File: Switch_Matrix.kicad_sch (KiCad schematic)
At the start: 151 parts, among them SW1 SW_Push_45deg, SW10 SW_Push_45deg, SW11 SW_Push_45deg, SW12 SW_Push_45deg, SW12(2)1 SW_Push_45deg, SW13 SW_Push_45deg, SW14 SW_Push_45deg, SW15 SW_Push_45deg, SW16 SW_Push_45deg, SW17 SW_Push_45deg, SW18 SW_Push_45deg, SW19 SW_Push_45deg, SW2 SW_Push_45deg, SW20 SW_Push_45deg, SW21 SW_Push_45deg, SW22 SW_Push_45deg, SW23 SW_Push_45deg, SW24 SW_Push_45deg, SW24(1.5)1 SW_Push_45deg, SW25 SW_Push_45deg, SW26 SW_Push_45deg, SW26(2)1 SW_Push_45deg, SW26(ISO)1 SW_Push_45deg, SW27(1.25)1 SW_Push_45deg, SW27(1.5)1 SW_Push_45deg, SW27(ortho)1 SW_Push_45deg, SW28 SW_Push_45deg, SW28(1.5stagger)1 SW_Push_45deg, SW28(ortho)1 SW_Push_45deg, SW29 SW_Push_45deg, SW29(1.5stagger)1 SW_Push_45deg, SW29(ortho)1 SW_Push_45deg, SW3 SW_Push_45deg, SW30 SW_Push_45deg, SW30(1.5stagger)1 SW_Push_45deg, SW30(ortho)1 SW_Push_45deg, SW31 SW_Push_45deg, SW31(1.5stagger)1 SW_Push_45deg, SW31(ortho)1 SW_Push_45deg, SW32 SW_Push_45deg, SW32(1.5stagger)1 SW_Push_45deg, SW32(ortho)1 SW_Push_45deg, SW33 SW_Push_45deg, SW33(1.5stagger)1 SW_Push_45deg, SW33(ortho)1 SW_Push_45deg, SW34 SW_Push_45deg, SW34(1.5stagger)1 SW_Push_45deg, SW34(ortho)1 SW_Push_45deg, SW35 SW_Push_45deg, SW35(1.5stagger)1 SW_Push_45deg, SW35(ortho)1 SW_Push_45deg, SW36 SW_Push_45deg, SW36(1.5stagger)1 SW_Push_45deg, SW36(ortho)1 SW_Push_45deg, SW37 SW_Push_45deg, SW37(1.5stagger)1 SW_Push_45deg, SW37(ortho)1 SW_Push_45deg, SW38(1.25)1 SW_Push_45deg, SW38(1.5)1 SW_Push_45deg, SW38(ortho)1 SW_Push_45deg, SW39 SW_Push_45deg, SW39(1.5)1 SW_Push_45deg, SW4 SW_Push_45deg, SW40 SW_Push_45deg, SW40(3)1 SW_Push_45deg, SW41 SW_Push_45deg, SW41(1.5)1 SW_Push_45deg, SW42(1)1 SW_Push_45deg, SW42(1.25)1 SW_Push_45deg, SW42(1.5)1 SW_Push_45deg, SW42(3)1 SW_Push_45deg, SW43(1.75)1 SW_Push_45deg, SW43(2)1 SW_Push_45deg, SW44(3)1 SW_Push_45deg, SW44(4)1 SW_Push_45deg, SW44(6)1 SW_Push_45deg, SW45(1.75)1 SW_Push_45deg, SW45(2)1 SW_Push_45deg, SW46(1)1 SW_Push_45deg, SW46(1.25)1 SW_Push_45deg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

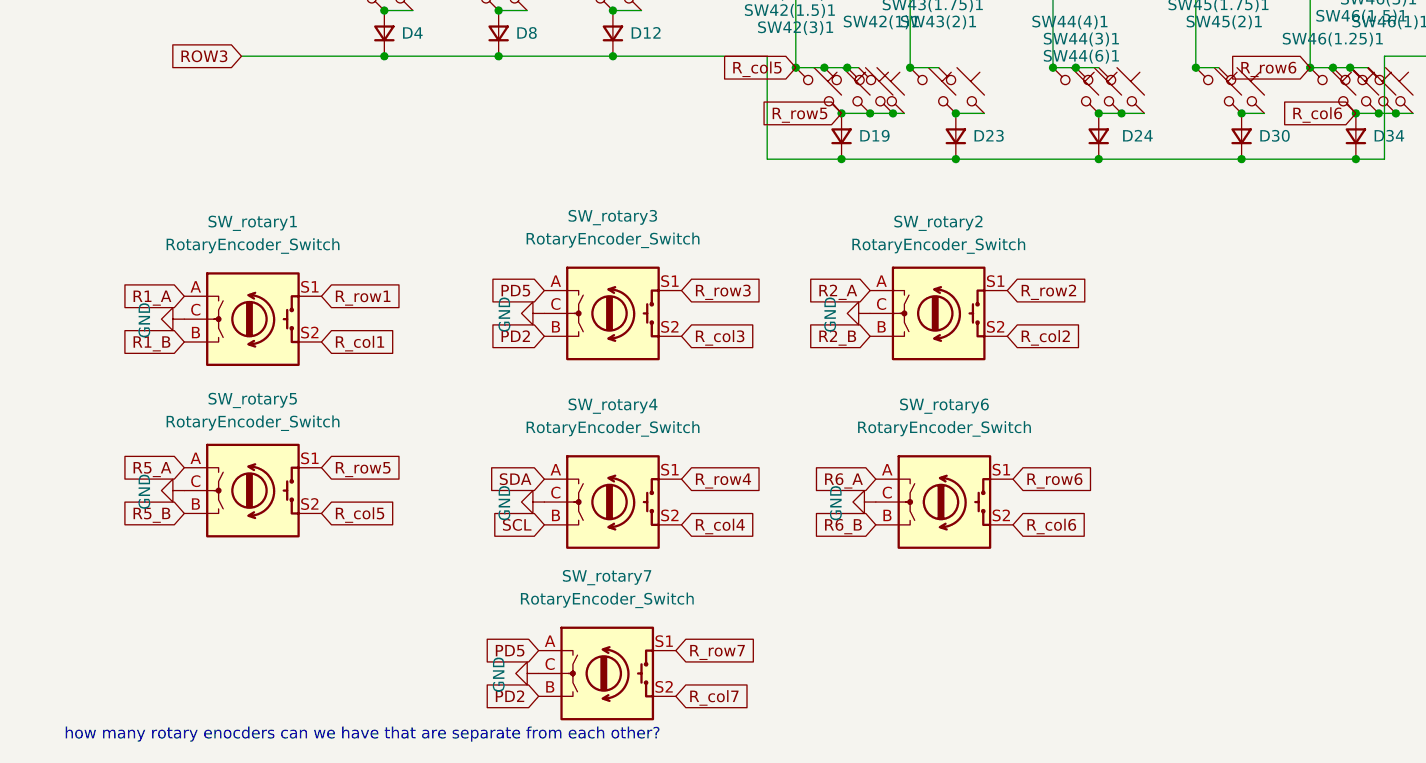
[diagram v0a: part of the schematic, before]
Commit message: finished prototype pcb
missing silkscreen, production files
needs clarification of some errors
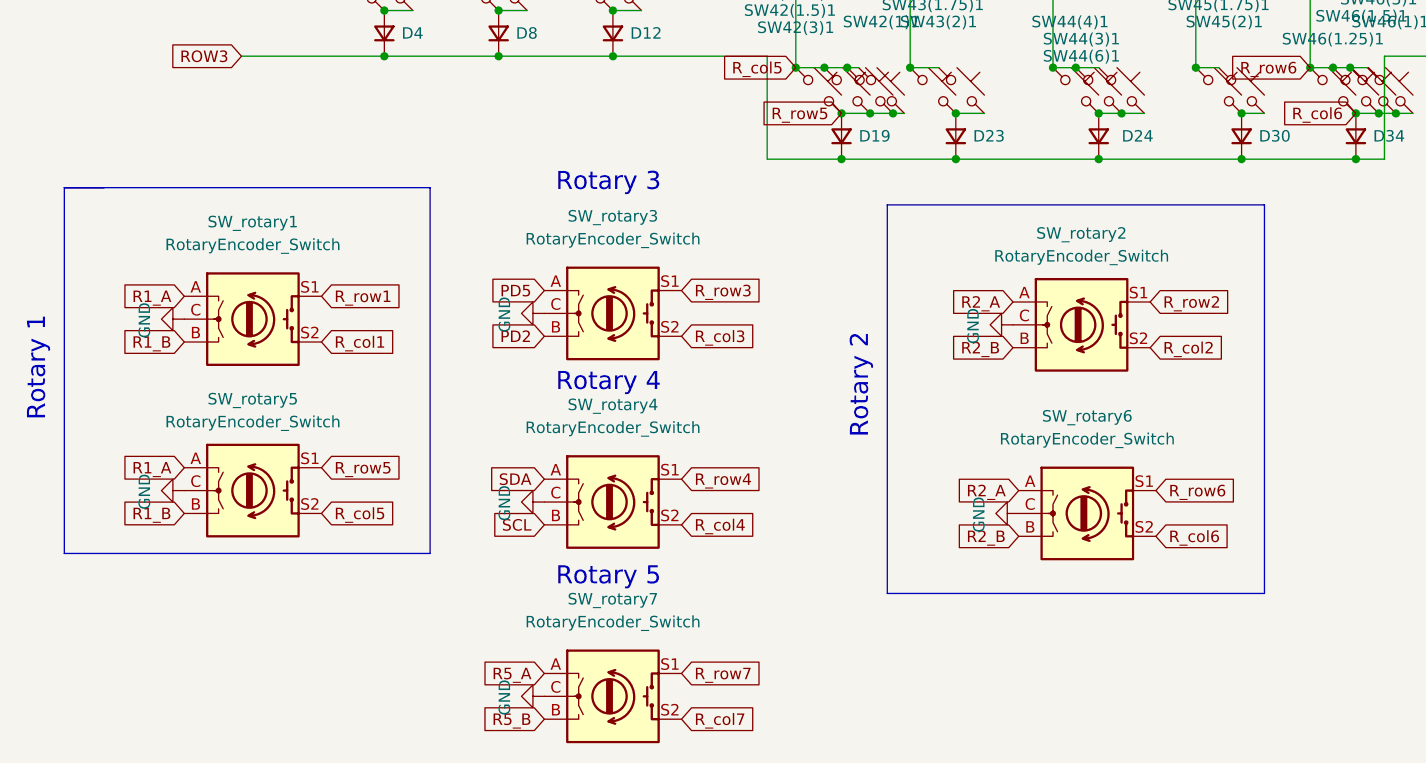
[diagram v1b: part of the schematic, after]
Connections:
- net R6_A is gone; now on net R2_A: SW_rotary6.A
- net R6_B is gone; now on net R2_B: SW_rotary6.B
- net PD2: no longer SW_rotary7.B
- net PD5: no longer SW_rotary7.A
- net R1_A: now also SW_rotary5.A
- net R1_B: now also SW_rotary5.B
- net R5_A: now also SW_rotary7.A; no longer SW_rotary5.A
- net R5_B: now also SW_rotary7.B; no longer SW_rotary5.B
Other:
- note added: "Rotary 1"
- note added: "Rotary 2"
- note added: "Rotary 3"
- note added: "Rotary 4"
- note added: "Rotary 5"
- note removed: "how many rotary enocders can we have that are separate from each other?"
- moved on the sheet: SW_rotary2, SW_rotary6, SW_rotary7

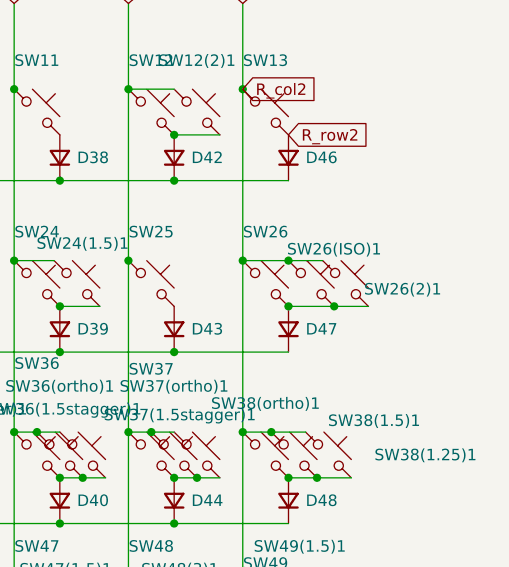
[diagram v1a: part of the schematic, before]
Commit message: added iso 1.5 key option, new production files
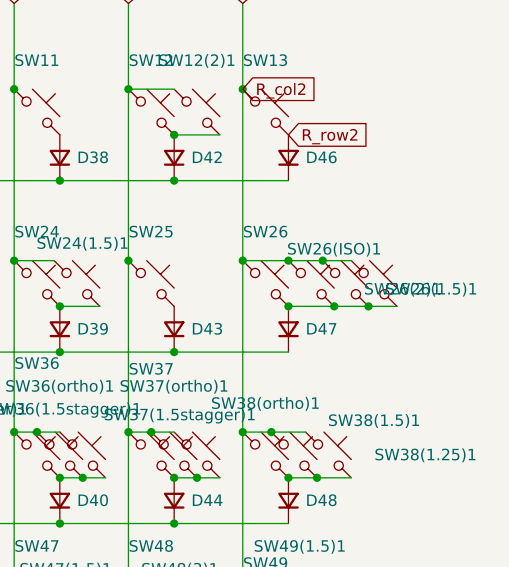
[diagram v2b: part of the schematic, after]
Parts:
- added SW26(1.5)1: SW_Push_45deg, MX_Only:MXOnly-1.5U-NoLED, symbol Switch:SW_Push_45deg
- SW26(ISO)1: footprint MX_Only:MXOnly-ISO-NoLED -> MX_Only:MXOnly-ISO-ReversedStabilizers-NoLED
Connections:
- net COL12: now also SW26(1.5)1.1
- net at D47.2 (A), SW26(2)1.2, SW26(ISO)1.2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: now also SW26(1.5)1.2
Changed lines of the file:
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@@
   (junction (at 214.63 106.045) (diameter 0) (color 0 0 0 0)
   )
+  (junction (at 223.52 69.215) (diameter 0) (color 0 0 0 0)
+  )
   (junction (at 219.71 74.295) (diameter 0) (color 0 0 0 0)
   )
@@
   (junction (at 189.23 88.265) (diameter 0) (color 0 0 0 0)
   )
+  (junction (at 228.6 74.295) (diameter 0) (color 0 0 0 0)
+  )
   (junction (at 86.36 93.345) (diameter 0) (color 0 0 0 0)
   )
@@
     (stroke (width 0) (type default) (color 0 0 0 0))
   )
+  (wire (pts (xy 228.6 74.295) (xy 231.775 74.295))
+    (stroke (width 0) (type default) (color 0 0 0 0))
+  )
   (wire (pts (xy 106.68 50.165) (xy 106.68 40.64))
     (stroke (width 0) (type default) (color 0 0 0 0))
@@
     (stroke (width 0) (type default) (color 0 0 0 0))
   )
+  (wire (pts (xy 223.52 69.215) (xy 226.695 69.215))
+    (stroke (width 0) (type default) (color 0 0 0 0))
+  )
   (wire (pts (xy 64.135 111.125) (xy 60.96 111.125))
     (stroke (width 0) (type default) (color 0 0 0 0))
@@
       (effects (font (size 1.27 1.27)) hide)
     )
-    (property "Footprint" "MX_Only:MXOnly-ISO-NoLED" (id 2) (at 222.25 71.755 0)
+    (property "Footprint" "MX_Only:MXOnly-ISO-ReversedStabilizers-NoLED" (id 2) (at 222.25 71.755 0)
       (effects (font (size 1.27 1.27)) hide)
     )
@@
       (effects (font (size 1.27 1.27)) hide)
     )
+    (pin "1")
+    (pin "2")
+  )
+  (symbol (lib_id "Switch:SW_Push_45deg") (at 229.235 71.755 0) (unit 1)
+    (in_bom yes) (on_board yes)
+    (property "Reference" "SW26(1.5)1" (id 0) (at 235.585 72.39 0))
+    (property "Value" "SW_Push_45deg" (id 1) (at 229.235 66.675 0)
+      (effects (font (size 1.27 1.27)) hide)
+    )
+    (property "Footprint" "MX_Only:MXOnly-1.5U-NoLED" (id 2) (at 229.235 71.755 0)
+      (effects (font (size 1.27 1.27)) hide)
+    )
+    (property "Datasheet" "~" (id 3) (at 229.235 71.755 0)
+      (effects (font (size 1.27 1.27)) hide)
+    )

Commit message: cleaning up main folder
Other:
- note added: "Rotary A"
- note added: "Rotary B"
- note added: "Rotary C"
- note added: "Rotary D"
- note added: "Rotary E"
- note removed: "Rotary 1"
- note removed: "Rotary 2"
- note removed: "Rotary 3"
- note removed: "Rotary 4"
- note removed: "Rotary 5"
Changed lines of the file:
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@@
     (stroke (width 0) (type default) (color 0 0 0 0))
   )
-  (text "Rotary 3" (at 80.01 131.445 0)
+  (text "Rotary C" (at 80.01 131.445 0)
     (effects (font (size 2 2)) (justify left bottom))
   )
-  (text "Rotary 2\n" (at 114.935 158.75 90)
+  (text "Rotary B" (at 114.935 158.75 90)
     (effects (font (size 2 2)) (justify left bottom))
   )
-  (text "Rotary 1" (at 23.495 156.845 90)
+  (text "Rotary A" (at 23.495 156.845 90)
     (effects (font (size 2 2)) (justify left bottom))
   )
-  (text "Rotary 5" (at 80.01 175.26 0)
+  (text "Rotary E" (at 80.01 175.26 0)
     (effects (font (size 2 2)) (justify left bottom))
   )
-  (text "Rotary 4" (at 80.01 153.67 0)
+  (text "Rotary D" (at 80.01 153.67 0)
     (effects (font (size 2 2)) (justify left bottom))
   )
